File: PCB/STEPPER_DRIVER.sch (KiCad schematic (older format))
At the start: 10 parts, among them J3 STEPPER, J4 STEPPER

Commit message: Added correct DRV breakout and added testpoints
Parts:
- removed A1: STEPPER_DRIVER_BREAKOUT, Module:Pololu_Breakout-16_15.2x20.3mm, symbol Driver_Motor:Pololu_Breakout_A4988
- added TP2: ~RESET, symbol Connector:TestPoint
- added TP3: ~SLEEP, symbol Connector:TestPoint
- added TP4: ~FAULT, symbol Connector:TestPoint
- added TP5: ~HOME, symbol Connector:TestPoint
- added TP6: DECAY, symbol Connector:TestPoint
- added U15: DRV8825_BREAKOUT, symbol custom:DRV8825_BREAKOUT
- JP1: value MS1 -> MS0
- JP2: value MS2 -> MS1
- JP3: value MS3 -> MS2
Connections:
- net labels added: DECAY, MS0, ~FAULT, ~HOME, ~RESET, ~SLEEP
- net labels removed: MS3
- wire segments 16 -> 17
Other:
- moved on the sheet: J7, J8

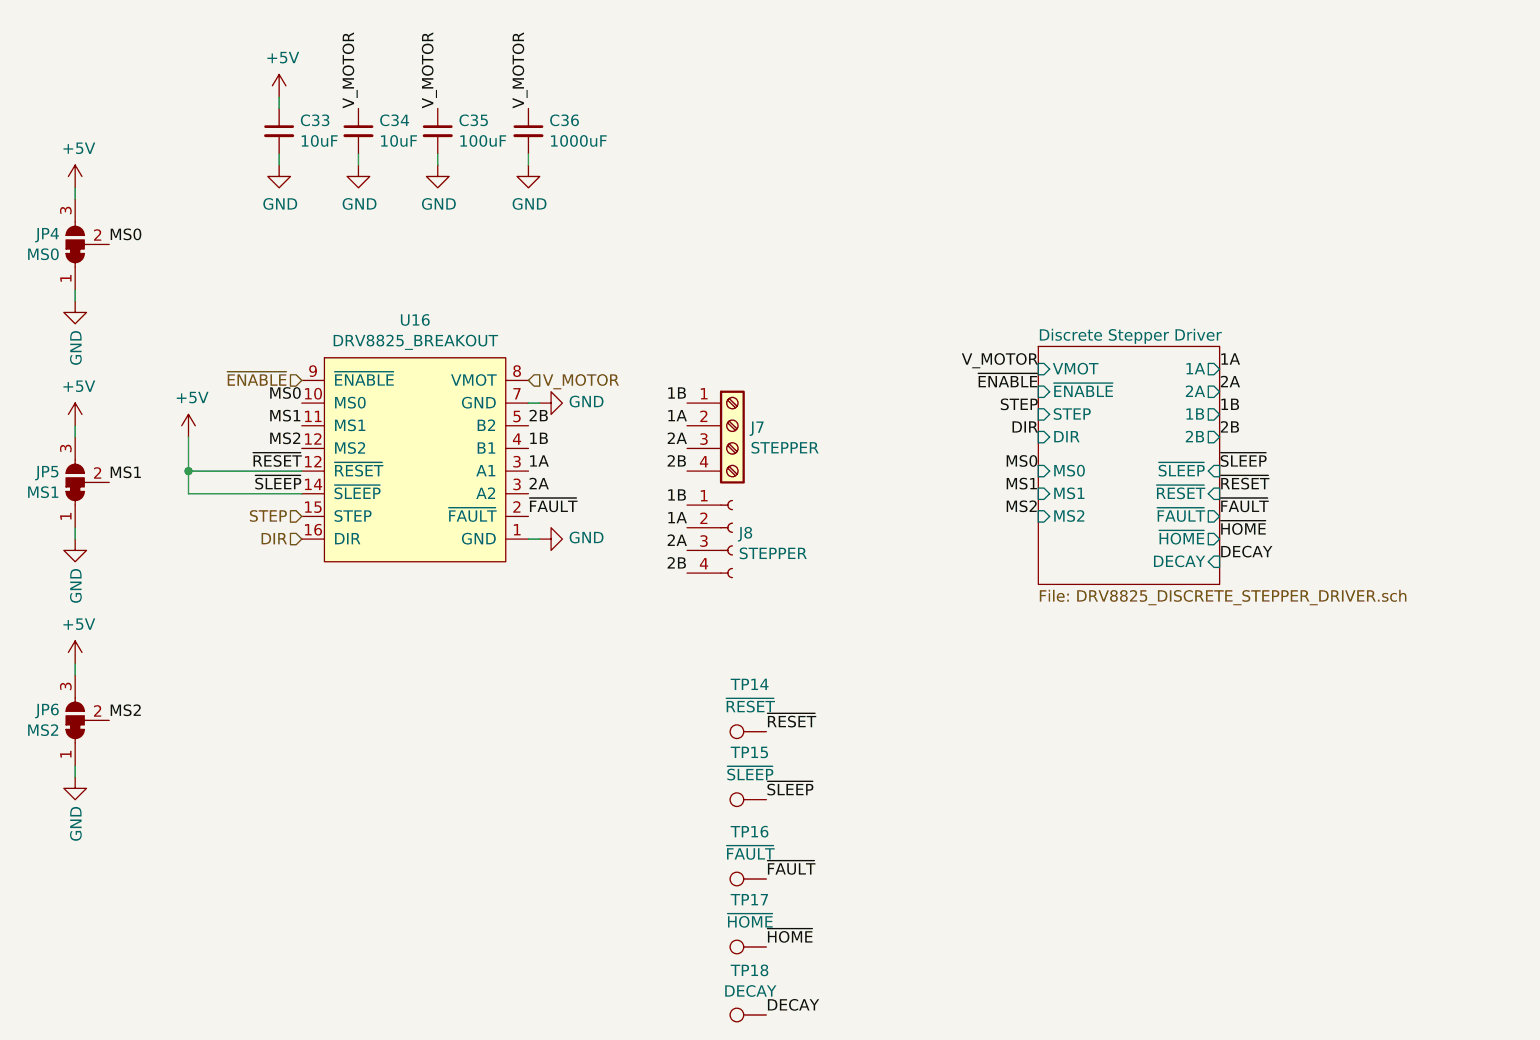
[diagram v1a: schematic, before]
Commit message: Added test points to PSU
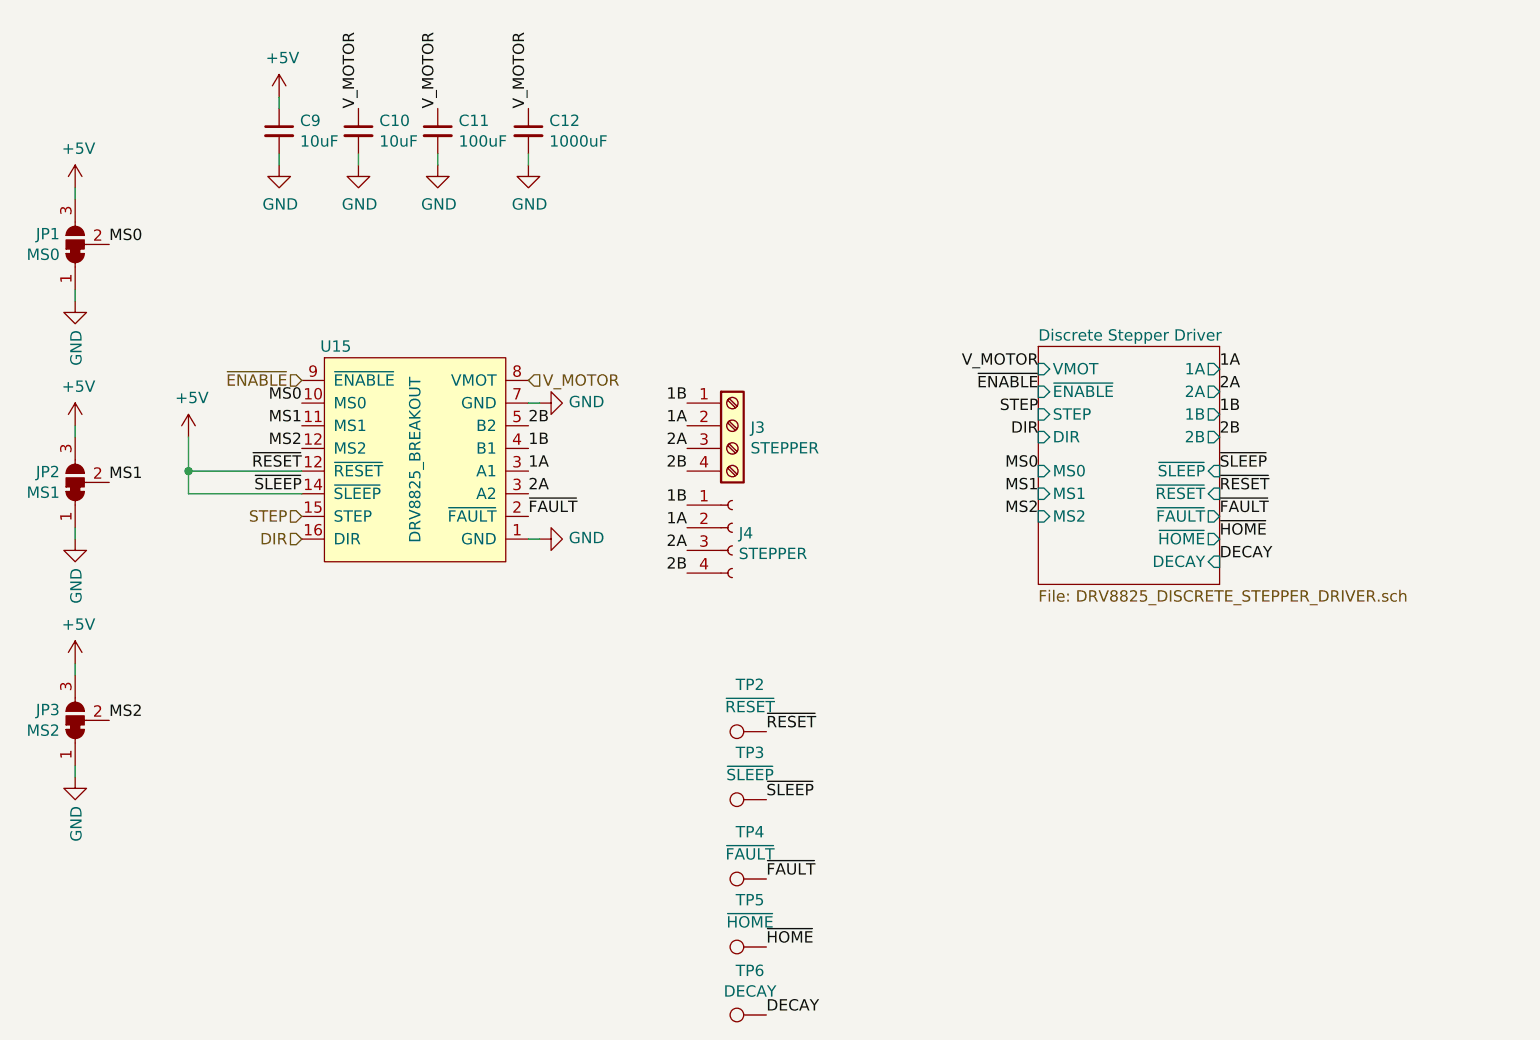
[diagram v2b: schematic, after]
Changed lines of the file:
@@
 AR Path="/5E8A6686/5E8A7820" Ref="J4"  Part="1"
 AR Path="/5E8813FF/5E8A7820" Ref="J8"  Part="1"
-F 0 "J8" H 7278 4226 50  0000 L CNN
+F 0 "J4" H 7278 4226 50  0000 L CNN
 F 1 "STEPPER" H 7278 4135 50  0000 L CNN
 F 2 "" H 7250 4250 50  0001 C CNN
@@
 AR Path="/5E8A6686/5E8A82D9" Ref="J3"  Part="1"
 AR Path="/5E8813FF/5E8A82D9" Ref="J7"  Part="1"
-F 0 "J7" H 7330 3792 50  0000 L CNN
+F 0 "J3" H 7330 3792 50  0000 L CNN
 F 1 "STEPPER" H 7330 3701 50  0000 L CNN
 F 2 "" H 7250 3800 50  0001 C CNN
@@
 AR Path="/5E8A6686/5E842853" Ref="#PWR034"  Part="1"
 AR Path="/5E8813FF/5E842853" Ref="#PWR0100"  Part="1"
-F 0 "#PWR0100" H 6400 4050 50  0001 C CNN
+F 0 "#PWR034" H 6400 4050 50  0001 C CNN
 F 1 "GND" V 6405 4172 50  0000 R CNN
 F 2 "" H 6400 4300 50  0001 C CNN
@@
 AR Path="/5E8A6686/5E842AD6" Ref="#PWR035"  Part="1"
 AR Path="/5E8813FF/5E842AD6" Ref="#PWR0101"  Part="1"
-F 0 "#PWR0101" H 6400 3450 50  0001 C CNN
+F 0 "#PWR035" H 6400 3450 50  0001 C CNN
 F 1 "GND" V 6405 3572 50  0000 R CNN
 F 2 "" H 6400 3700 50  0001 C CNN
@@
 AR Path="/5E8A6686/5E8548E0" Ref="C11"  Part="1"
 AR Path="/5E8813FF/5E8548E0" Ref="C35"  Part="1"
-F 0 "C35" H 6042 2546 50  0000 L CNN
+F 0 "C11" H 6042 2546 50  0000 L CNN
 F 1 "100uF" H 6042 2455 50  0000 L CNN
 F 2 "" H 5950 2500 50  0001 C CNN
@@
 AR Path="/5E8A6686/5E8548E7" Ref="#PWR036"  Part="1"
 AR Path="/5E8813FF/5E8548E7" Ref="#PWR0102"  Part="1"
-F 0 "#PWR0102" H 5950 2400 50  0001 C CNN
+F 0 "#PWR036" H 5950 2400 50  0001 C CNN
 F 1 "GND" H 5955 2477 50  0000 C CNN
 F 2 "" H 5950 2650 50  0001 C CNN
@@
 AR Path="/5E8A6686/5E8572F7" Ref="C10"  Part="1"
 AR Path="/5E8813FF/5E8572F7" Ref="C34"  Part="1"
-F 0 "C34" H 5692 2546 50  0000 L CNN
+F 0 "C10" H 5692 2546 50  0000 L CNN
 F 1 "10uF" H 5692 2455 50  0000 L CNN
 F 2 "" H 5600 2500 50  0001 C CNN
@@
 AR Path="/5E8A6686/5E8572FE" Ref="#PWR032"  Part="1"
 AR Path="/5E8813FF/5E8572FE" Ref="#PWR098"  Part="1"
-F 0 "#PWR098" H 5600 2400 50  0001 C CNN
+F 0 "#PWR032" H 5600 2400 50  0001 C CNN
 F 1 "GND" H 5605 2477 50  0000 C CNN
 F 2 "" H 5600 2650 50  0001 C CNN
@@
 AR Path="/5E8A6686/5E860421" Ref="C9"  Part="1"
 AR Path="/5E8813FF/5E860421" Ref="C33"  Part="1"
-F 0 "C33" H 5342 2546 50  0000 L CNN
+F 0 "C9" H 5342 2546 50  0000 L CNN
 F 1 "10uF" H 5342 2455 50  0000 L CNN
 F 2 "" H 5250 2500 50  0001 C CNN
@@
 AR Path="/5E8A6686/5E860428" Ref="#PWR026"  Part="1"
 AR Path="/5E8813FF/5E860428" Ref="#PWR092"  Part="1"
-F 0 "#PWR092" H 5250 2400 50  0001 C CNN
+F 0 "#PWR026" H 5250 2400 50  0001 C CNN
 F 1 "GND" H 5255 2477 50  0000 C CNN
 F 2 "" H 5250 2650 50  0001 C CNN
@@
 AR Path="/5E8A6686/5E90606A" Ref="#PWR025"  Part="1"
 AR Path="/5E8813FF/5E90606A" Ref="#PWR091"  Part="1"
-F 0 "#PWR091" H 5250 2200 50  0001 C CNN
+F 0 "#PWR025" H 5250 2200 50  0001 C CNN
 F 1 "+5V" H 5265 2523 50  0000 C CNN
 F 2 "" H 5250 2350 50  0001 C CNN
@@
 AR Path="/5E8A6686/5E85775C" Ref="#PWR037"  Part="1"
 AR Path="/5E8813FF/5E85775C" Ref="#PWR0103"  Part="1"
-F 0 "#PWR0103" H 6350 2400 50  0001 C CNN
+F 0 "#PWR037" H 6350 2400 50  0001 C CNN
 F 1 "GND" H 6355 2477 50  0000 C CNN
 F 2 "" H 6350 2650 50  0001 C CNN
@@
 AR Path="/5E8A6686/5E857755" Ref="C12"  Part="1"
 AR Path="/5E8813FF/5E857755" Ref="C36"  Part="1"
-F 0 "C36" H 6442 2546 50  0000 L CNN
+F 0 "C12" H 6442 2546 50  0000 L CNN
 F 1 "1000uF" H 6442 2455 50  0000 L CNN
 F 2 "" H 6350 2500 50  0001 C CNN
@@
 AR Path="/5E8A6686/5E913339" Ref="JP1"  Part="1"
 AR Path="/5E8813FF/5E913339" Ref="JP4"  Part="1"
-F 0 "JP4" V 4396 3068 50  0000 L CNN
+F 0 "JP1" V 4396 3068 50  0000 L CNN
 F 1 "MS0" V 4305 3068 50  0000 L CNN
 F 2 "" H 4350 3000 50  0001 C CNN
@@
 AR Path="/5E8A6686/5E9143CE" Ref="#PWR09"  Part="1"
 AR Path="/5E8813FF/5E9143CE" Ref="#PWR044"  Part="1"
-F 0 "#PWR044" H 4350 2600 50  0001 C CNN
+F 0 "#PWR09" H 4350 2600 50  0001 C CNN
 F 1 "+5V" H 4365 2923 50  0000 C CNN
 F 2 "" H 4350 2750 50  0001 C CNN
@@
 AR Path="/5E8A6686/5E914CAC" Ref="#PWR029"  Part="1"
 AR Path="/5E8813FF/5E914CAC" Ref="#PWR095"  Part="1"
-F 0 "#PWR095" H 4350 3000 50  0001 C CNN
+F 0 "#PWR029" H 4350 3000 50  0001 C CNN
 F 1 "GND" V 4355 3122 50  0000 R CNN
 F 2 "" H 4350 3250 50  0001 C CNN
@@
 AR Path="/5E8A6686/5E916887" Ref="JP2"  Part="1"
 AR Path="/5E8813FF/5E916887" Ref="JP5"  Part="1"
-F 0 "JP5" V 4396 4118 50  0000 L CNN
+F 0 "JP2" V 4396 4118 50  0000 L CNN
 F 1 "MS1" V 4305 4118 50  0000 L CNN
 F 2 "" H 4350 4050 50  0001 C CNN
@@
 AR Path="/5E8A6686/5E91688D" Ref="#PWR030"  Part="1"
 AR Path="/5E8813FF/5E91688D" Ref="#PWR096"  Part="1"
-F 0 "#PWR096" H 4350 3650 50  0001 C CNN
+F 0 "#PWR030" H 4350 3650 50  0001 C CNN
 F 1 "+5V" H 4365 3973 50  0000 C CNN
 F 2 "" H 4350 3800 50  0001 C CNN
@@
 AR Path="/5E8A6686/5E916894" Ref="#PWR031"  Part="1"
 AR Path="/5E8813FF/5E916894" Ref="#PWR097"  Part="1"
-F 0 "#PWR097" H 4350 4050 50  0001 C CNN
+F 0 "#PWR031" H 4350 4050 50  0001 C CNN
 F 1 "GND" V 4355 4172 50  0000 R CNN
 F 2 "" H 4350 4300 50  0001 C CNN
@@
 AR Path="/5E8A6686/5E917232" Ref="JP3"  Part="1"
 AR Path="/5E8813FF/5E917232" Ref="JP6"  Part="1"
-F 0 "JP6" V 4396 5168 50  0000 L CNN
+F 0 "JP3" V 4396 5168 50  0000 L CNN
 F 1 "MS2" V 4305 5168 50  0000 L CNN
 F 2 "" H 4350 5100 50  0001 C CNN
@@
 AR Path="/5E8A6686/5E917238" Ref="#PWR042"  Part="1"
 AR Path="/5E8813FF/5E917238" Ref="#PWR0108"  Part="1"
-F 0 "#PWR0108" H 4350 4700 50  0001 C CNN
+F 0 "#PWR042" H 4350 4700 50  0001 C CNN
 F 1 "+5V" H 4365 5023 50  0000 C CNN
 F 2 "" H 4350 4850 50  0001 C CNN
@@
 AR Path="/5E8A6686/5E91723F" Ref="#PWR043"  Part="1"
 AR Path="/5E8813FF/5E91723F" Ref="#PWR0109"  Part="1"
-F 0 "#PWR0109" H 4350 5100 50  0001 C CNN
+F 0 "#PWR043" H 4350 5100 50  0001 C CNN
 F 1 "GND" V 4355 5222 50  0000 R CNN
 F 2 "" H 4350 5350 50  0001 C CNN
@@
 AR Path="/5E8A6686/5E952808" Ref="#PWR027"  Part="1"
 AR Path="/5E8813FF/5E952808" Ref="#PWR028"  Part="1"
-F 0 "#PWR028" H 4850 3700 50  0001 C CNN
+F 0 "#PWR027" H 4850 3700 50  0001 C CNN
 F 1 "+5V" H 4865 4023 50  0000 C CNN
 F 2 "" H 4850 3850 50  0001 C CNN
@@
 AR Path="/5E8A6686/5E972E18" Ref="U15"  Part="1"
 AR Path="/5E8813FF/5E972E18" Ref="U16"  Part="1"
-F 0 "U16" H 5850 4565 50  0000 C CNN
-F 1 "DRV8825_BREAKOUT" H 5850 4474 50  0000 C CNN
+F 0 "U15" H 5500 4450 50  0000 C CNN
+F 1 "DRV8825_BREAKOUT" V 5850 3950 50  0000 C CNN
 F 2 "" H 6000 3900 50  0001 C CNN
 F 3 "" H 6000 3900 50  0001 C CNN
@@
 AR Path="/5E8A6686/5E9970FA" Ref="TP2"  Part="1"
 AR Path="/5E8813FF/5E9970FA" Ref="TP14"  Part="1"
-F 0 "TP14" V 7607 5222 50  0000 C CNN
+F 0 "TP2" V 7607 5222 50  0000 C CNN
 F 1 "~RESET" V 7509 5222 50  0000 C CNN
 F 2 "" H 7600 5150 50  0001 C CNN
@@
 AR Path="/5E8A6686/5E9975F2" Ref="TP3"  Part="1"
 AR Path="/5E8813FF/5E9975F2" Ref="TP15"  Part="1"
-F 0 "TP15" V 7607 5522 50  0000 C CNN
+F 0 "TP3" V 7607 5522 50  0000 C CNN
 F 1 "~SLEEP" V 7509 5522 50  0000 C CNN
 F 2 "" H 7600 5450 50  0001 C CNN
@@
 AR Path="/5E8A6686/5E998E5E" Ref="TP4"  Part="1"
 AR Path="/5E8813FF/5E998E5E" Ref="TP16"  Part="1"
-F 0 "TP16" V 7607 5872 50  0000 C CNN
+F 0 "TP4" V 7607 5872 50  0000 C CNN
 F 1 "~FAULT" V 7509 5872 50  0000 C CNN
 F 2 "" H 7600 5800 50  0001 C CNN
@@
 AR Path="/5E8A6686/5E998E64" Ref="TP5"  Part="1"
 AR Path="/5E8813FF/5E998E64" Ref="TP17"  Part="1"
-F 0 "TP17" V 7607 6172 50  0000 C CNN
+F 0 "TP5" V 7607 6172 50  0000 C CNN
 F 1 "~HOME" V 7509 6172 50  0000 C CNN
 F 2 "" H 7600 6100 50  0001 C CNN
@@
 AR Path="/5E8A6686/5E99966E" Ref="TP6"  Part="1"
 AR Path="/5E8813FF/5E99966E" Ref="TP18"  Part="1"
-F 0 "TP18" V 7595 6472 50  0000 C CNN
+F 0 "TP6" V 7595 6472 50  0000 C CNN
 F 1 "DECAY" V 7504 6472 50  0000 C CNN
 F 2 "" H 7600 6400 50  0001 C CNN

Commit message: Added remaining test points
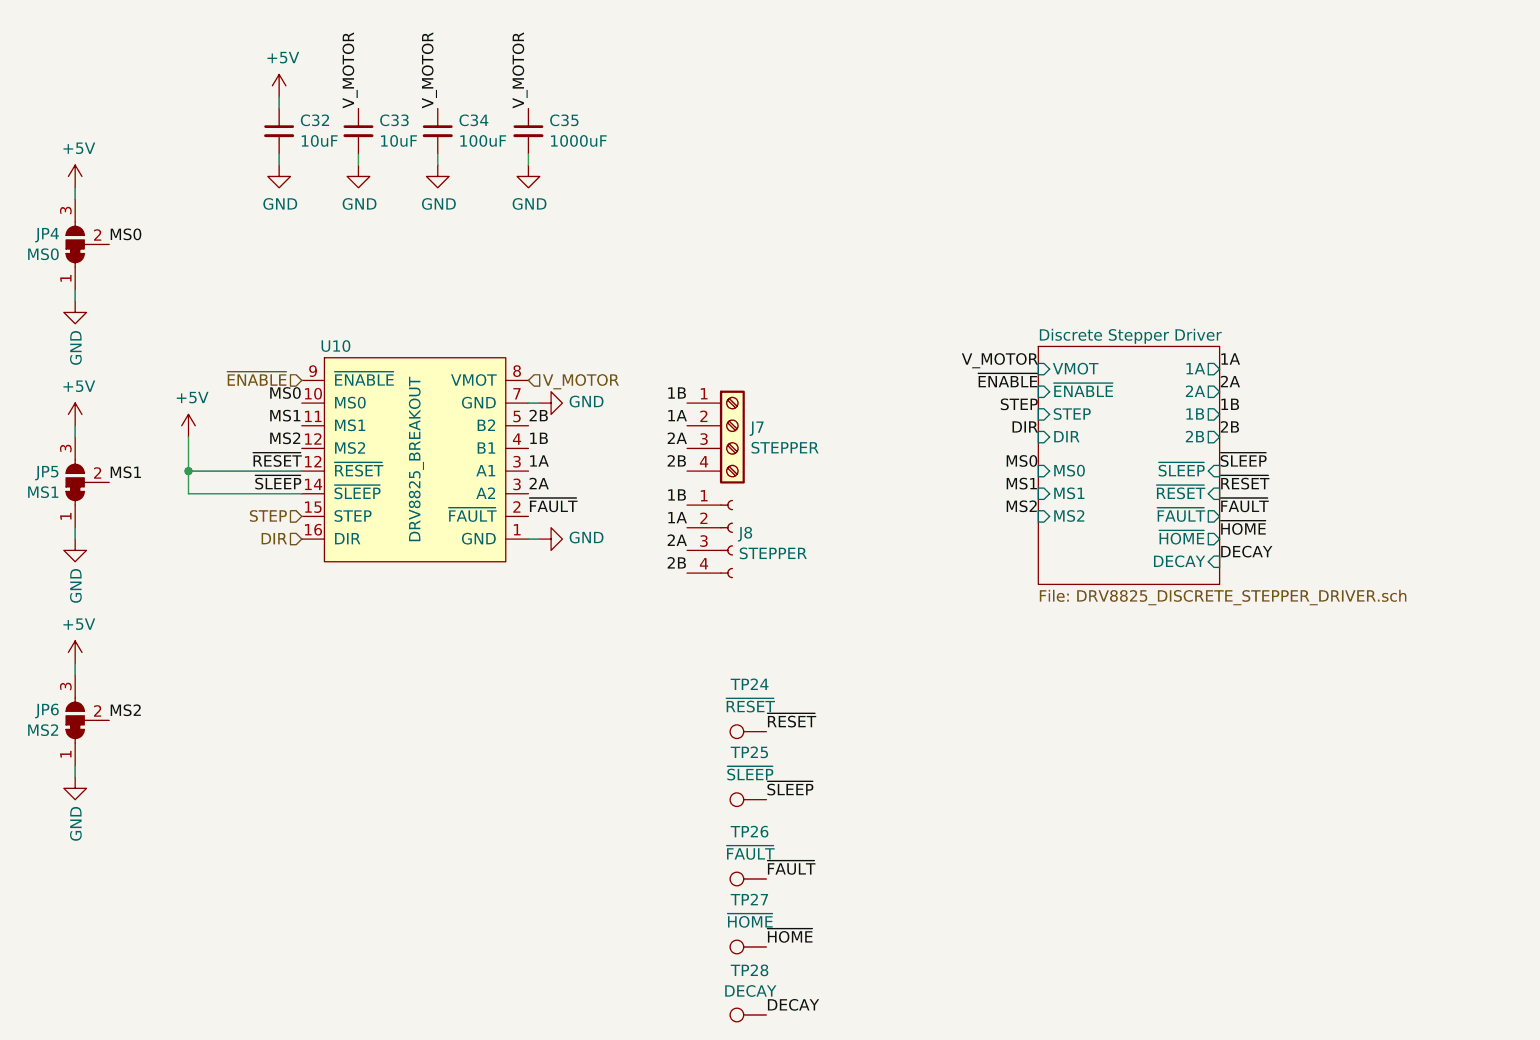
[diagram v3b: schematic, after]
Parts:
- renumbered C12 to C10, C9 to C7, C10 to C8, C11 to C9, TP6 to TP10, TP2 to TP6, TP3 to TP7, TP4 to TP8, TP5 to TP9, U15 to U3
